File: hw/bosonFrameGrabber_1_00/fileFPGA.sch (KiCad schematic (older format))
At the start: 16 parts, among them U3 ICE40HX8K, X1 ASDMB

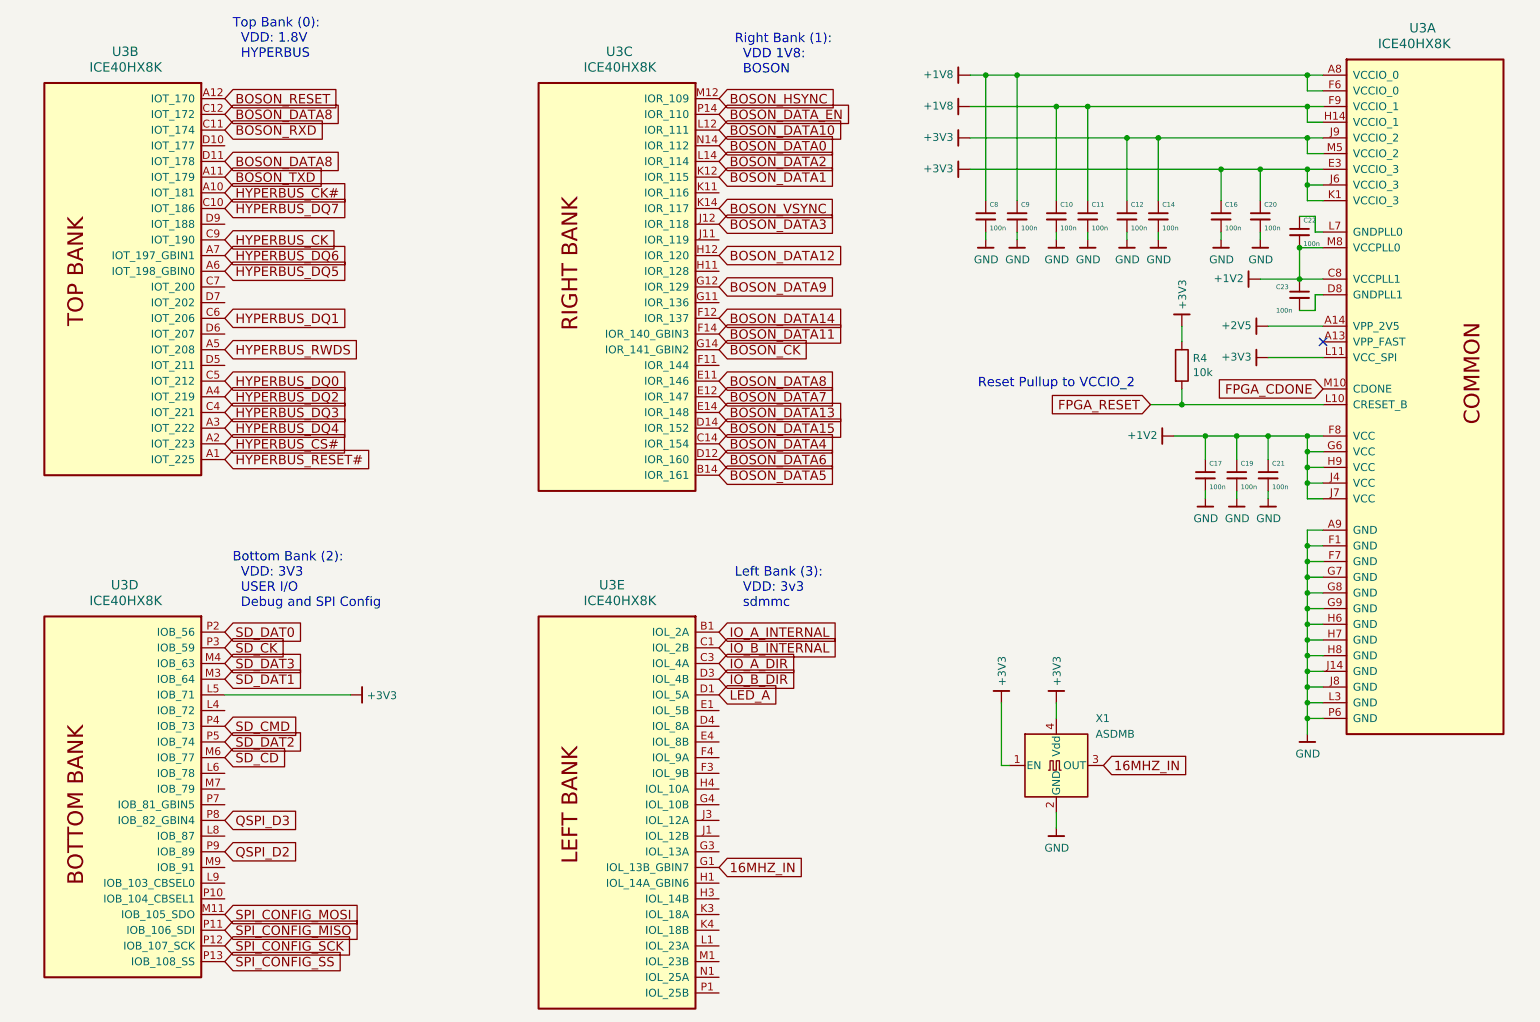
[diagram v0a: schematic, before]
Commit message: Update PCB with new footprint. Code project for bosonBreakout. (samd51) Simulation code for Verilog HyperRam module.
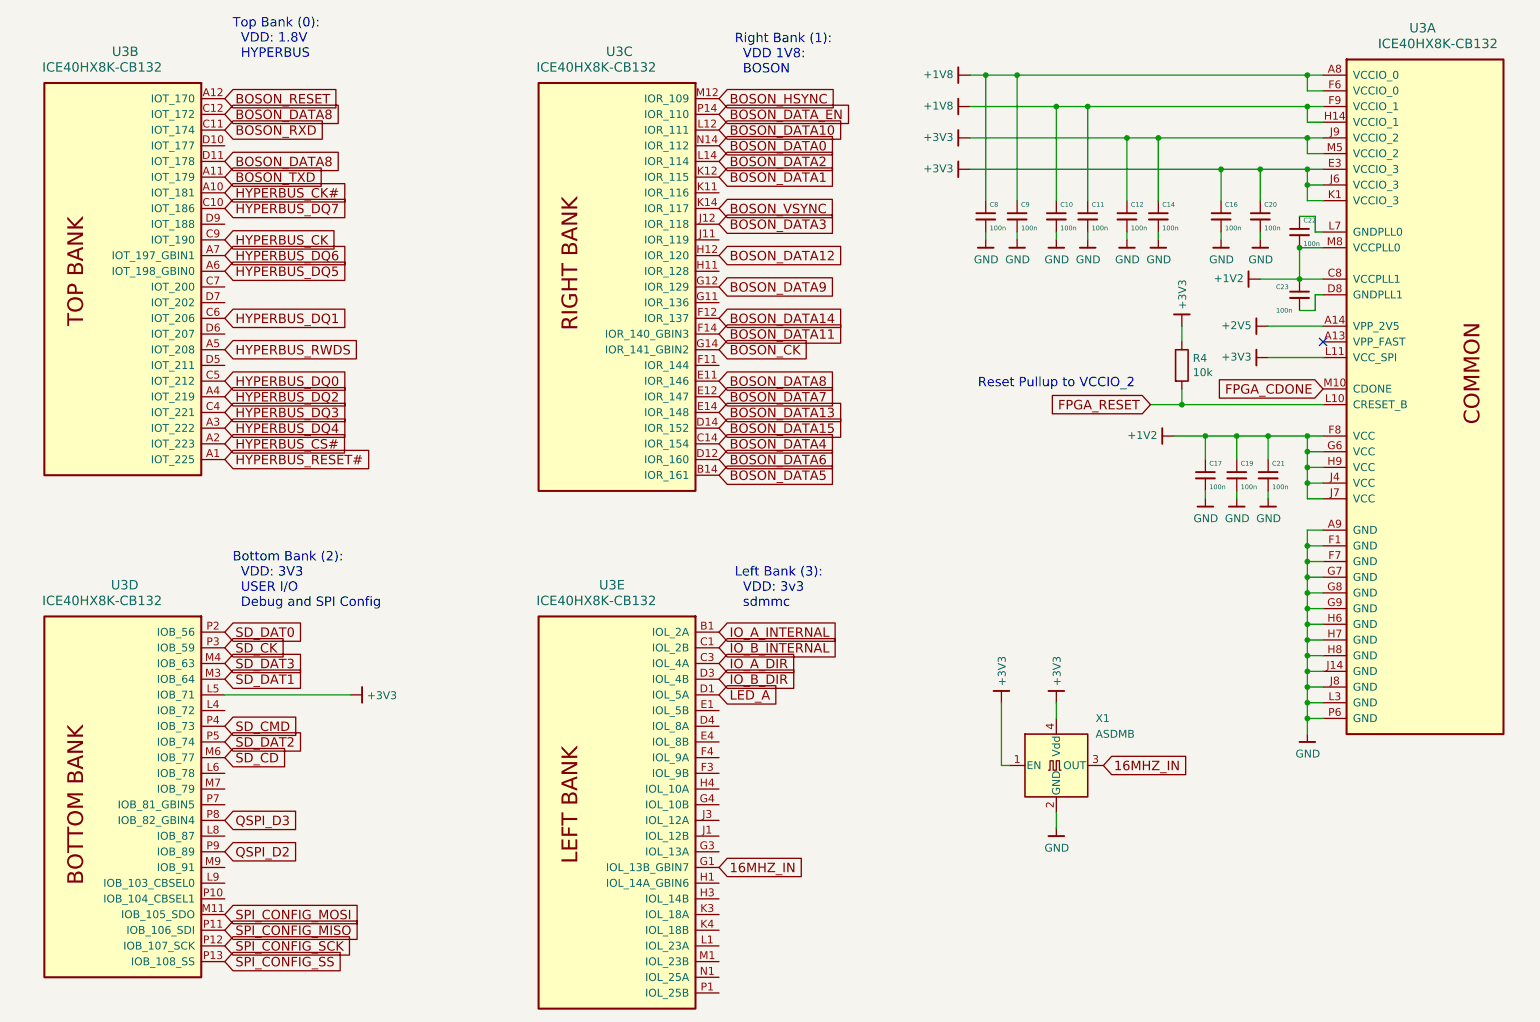
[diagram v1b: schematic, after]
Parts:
- C10, C11, C12, C14, C16, C17, C19, C20, C21, C22, C23, C8, C9: PN (none) -> CL05B104KP5NNNC; SN-DK (none) -> 1276-1002-1-ND
- R4: PN (none) -> ERA-2AED103X; SN-DK (none) -> P10KDECT-ND
- U3: value ICE40HX8K -> ICE40HX8K-CB132; PN (none) -> ICE40HX8K-CB132; SN-DK (none) -> 220-1577-ND
- X1: PN (none) -> ASDMB-24.000MHZ-LC-T; SN-DK (none) -> 535-11728-1-ND
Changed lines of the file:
@@
 EESchema Schematic File Version 4
+LIBS:bosonFrameGrabber-cache
 EELAYER 26 0
 EELAYER END
@@
 P 10100 2100
 F 0 "U3" H 10000 3050 60  0000 L CNN
-F 1 "ICE40HX8K" H 9800 2950 60  0000 L CNN
+F 1 " ICE40HX8K-CB132 " H 9800 2950 60  0000 L CNN
 F 2 "bosonFrameGrabber:csBGA_132" H 10100 2900 60  0001 C CNN
 F 3 "" H 10100 2900 60  0001 C CNN
+F 4 " 220-1577-ND " H 0   0   50  0001 C CNN "SN-DK"
+F 5 " ICE40HX8K-CB132 " H 0   0   50  0001 C CNN "PN"
 	1    10100 2100
 	1    0    0    -1
@@
 P 1800 2250
 F 0 "U3" H 1700 3200 60  0000 L CNN
-F 1 "ICE40HX8K" H 1550 3100 60  0000 L CNN
+F 1 " ICE40HX8K-CB132 " H 1550 3100 60  0000 L CNN
 F 2 "bosonFrameGrabber:csBGA_132" H 1800 3050 60  0001 C CNN
 F 3 "" H 1800 3050 60  0001 C CNN
+F 4 " 220-1577-ND " H 0   0   50  0001 C CNN "SN-DK"
+F 5 " ICE40HX8K-CB132 " H 0   0   50  0001 C CNN "PN"
 	2    1800 2250
 	-1   0    0    -1
@@
 P 4950 2250
 F 0 "U3" H 4850 3200 60  0000 L CNN
-F 1 "ICE40HX8K" H 4700 3100 60  0000 L CNN
+F 1 " ICE40HX8K-CB132 " H 4700 3100 60  0000 L CNN
 F 2 "bosonFrameGrabber:csBGA_132" H 4950 3050 60  0001 C CNN
 F 3 "" H 4950 3050 60  0001 C CNN
+F 4 " 220-1577-ND " H 0   0   50  0001 C CNN "SN-DK"
+F 5 " ICE40HX8K-CB132 " H 0   0   50  0001 C CNN "PN"
 	3    4950 2250
 	-1   0    0    -1
@@
 P 1800 5650
 F 0 "U3" H 1700 6600 60  0000 L CNN
-F 1 "ICE40HX8K" H 1550 6500 60  0000 L CNN
+F 1 " ICE40HX8K-CB132 " H 1550 6500 60  0000 L CNN
 F 2 "bosonFrameGrabber:csBGA_132" H 1800 6450 60  0001 C CNN
 F 3 "" H 1800 6450 60  0001 C CNN
+F 4 " 220-1577-ND " H 0   0   50  0001 C CNN "SN-DK"
+F 5 " ICE40HX8K-CB132 " H 0   0   50  0001 C CNN "PN"
 	4    1800 5650
 	-1   0    0    -1
@@
 P 4950 5650
 F 0 "U3" H 4900 6600 60  0000 L CNN
-F 1 "ICE40HX8K" H 4700 6500 60  0000 L CNN
+F 1 " ICE40HX8K-CB132 " H 4700 6500 60  0000 L CNN
 F 2 "bosonFrameGrabber:csBGA_132" H 4950 6450 60  0001 C CNN
 F 3 "" H 4950 6450 60  0001 C CNN
+F 4 " 220-1577-ND " H 0   0   50  0001 C CNN "SN-DK"
+F 5 " ICE40HX8K-CB132 " H 0   0   50  0001 C CNN "PN"
 	5    4950 5650
 	-1   0    0    -1
@@
 F 2 "Capacitors_SMD:C_0402" H 9050 2350 50  0001 C CNN
 F 3 "" H 9050 2350 50  0001 C CNN
+F 4 " 1276-1002-1-ND " H 0   0   50  0001 C CNN "SN-DK"
+F 5 " CL05B104KP5NNNC " H 0   0   50  0001 C CNN "PN"
 	1    9050 2350
 	1    0    0    -1
@@
 F 2 "Capacitors_SMD:C_0402" H 8800 2350 50  0001 C CNN
 F 3 "" H 8800 2350 50  0001 C CNN
+F 4 " 1276-1002-1-ND " H 0   0   50  0001 C CNN "SN-DK"
+F 5 " CL05B104KP5NNNC " H 0   0   50  0001 C CNN "PN"
 	1    8800 2350
 	1    0    0    -1
@@
 F 2 "Capacitors_SMD:C_0402" H 8400 2350 50  0001 C CNN
 F 3 "" H 8400 2350 50  0001 C CNN
+F 4 " 1276-1002-1-ND " H 0   0   50  0001 C CNN "SN-DK"
+F 5 " CL05B104KP5NNNC " H 0   0   50  0001 C CNN "PN"
 	1    8400 2350
 	1    0    0    -1
@@
 F 2 "Capacitors_SMD:C_0402" H 8200 2350 50  0001 C CNN
 F 3 "" H 8200 2350 50  0001 C CNN
+F 4 " 1276-1002-1-ND " H 0   0   50  0001 C CNN "SN-DK"
+F 5 " CL05B104KP5NNNC " H 0   0   50  0001 C CNN "PN"
 	1    8200 2350
 	1    0    0    -1
@@
 F 2 "Capacitors_SMD:C_0402" H 7950 2350 50  0001 C CNN
 F 3 "" H 7950 2350 50  0001 C CNN
+F 4 " 1276-1002-1-ND " H 0   0   50  0001 C CNN "SN-DK"
+F 5 " CL05B104KP5NNNC " H 0   0   50  0001 C CNN "PN"
 	1    7950 2350
 	1    0    0    -1
@@
 F 2 "Capacitors_SMD:C_0402" H 7750 2350 50  0001 C CNN
 F 3 "" H 7750 2350 50  0001 C CNN
+F 4 " 1276-1002-1-ND " H 0   0   50  0001 C CNN "SN-DK"
+F 5 " CL05B104KP5NNNC " H 0   0   50  0001 C CNN "PN"
 	1    7750 2350
 	1    0    0    -1
@@
 F 2 "Capacitors_SMD:C_0402" H 7500 2350 50  0001 C CNN
 F 3 "" H 7500 2350 50  0001 C CNN
+F 4 " 1276-1002-1-ND " H 0   0   50  0001 C CNN "SN-DK"
+F 5 " CL05B104KP5NNNC " H 0   0   50  0001 C CNN "PN"
 	1    7500 2350
 	1    0    0    -1
@@
 F 2 "Capacitors_SMD:C_0402" H 7300 2350 50  0001 C CNN
 F 3 "" H 7300 2350 50  0001 C CNN
+F 4 " 1276-1002-1-ND " H 0   0   50  0001 C CNN "SN-DK"
+F 5 " CL05B104KP5NNNC " H 0   0   50  0001 C CNN "PN"
 	1    7300 2350
 	1    0    0    -1
@@
 F 2 "Capacitors_SMD:C_0402" H 9100 4000 50  0001 C CNN
 F 3 "" H 9100 4000 50  0001 C CNN
+F 4 " 1276-1002-1-ND " H 0   0   50  0001 C CNN "SN-DK"
+F 5 " CL05B104KP5NNNC " H 0   0   50  0001 C CNN "PN"
 	1    9100 4000
 	1    0    0    -1
@@
 F 2 "Capacitors_SMD:C_0402" H 8900 4000 50  0001 C CNN
 F 3 "" H 8900 4000 50  0001 C CNN
+F 4 " 1276-1002-1-ND " H 0   0   50  0001 C CNN "SN-DK"
+F 5 " CL05B104KP5NNNC " H 0   0   50  0001 C CNN "PN"
 	1    8900 4000
 	1    0    0    -1
@@
 F 2 "Capacitors_SMD:C_0402" H 8700 4000 50  0001 C CNN
 F 3 "" H 8700 4000 50  0001 C CNN
+F 4 " 1276-1002-1-ND " H 0   0   50  0001 C CNN "SN-DK"
+F 5 " CL05B104KP5NNNC " H 0   0   50  0001 C CNN "PN"
 	1    8700 4000
 	1    0    0    -1
@@
 F 2 "Capacitors_SMD:C_0402" H 9300 2450 50  0001 C CNN
 F 3 "" H 9300 2450 50  0001 C CNN
+F 4 " 1276-1002-1-ND " H 0   0   50  0001 C CNN "SN-DK"
+F 5 " CL05B104KP5NNNC " H 0   0   50  0001 C CNN "PN"
 	1    9300 2450
 	1    0    0    -1
@@
 F 2 "Capacitors_SMD:C_0402" H 9300 2850 50  0001 C CNN
 F 3 "" H 9300 2850 50  0001 C CNN
+F 4 " 1276-1002-1-ND " H 0   0   50  0001 C CNN "SN-DK"
+F 5 " CL05B104KP5NNNC " H 0   0   50  0001 C CNN "PN"
 	1    9300 2850
 	1    0    0    -1
@@
 F 2 "Oscillators:Oscillator_SMD_SeikoEpson_SG210-4pin_2.5x2.0mm" H 8450 5500 50  0001 C CNN
 F 3 "http://www.abracon.com/Oscillators/ASV.pdf" H 7650 5850 50  0001 C CNN
+F 4 " 535-11728-1-ND " H 0   0   50  0001 C CNN "SN-DK"
+F 5 " ASDMB-24.000MHZ-LC-T " H 0   0   50  0001 C CNN "PN"
 	1    7750 5850
 	1    0    0    -1
@@
 F 2 "Resistors_SMD:R_0402" V 8480 3300 50  0001 C CNN
 F 3 "" H 8550 3300 50  0001 C CNN
+F 4 " P10KDECT-ND " H 0   0   50  0001 C CNN "SN-DK"
+F 5 " ERA-2AED103X " H 0   0   50  0001 C CNN "PN"
 	1    8550 3300
 	1    0    0    -1
